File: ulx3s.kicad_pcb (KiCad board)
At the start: 4 copper layers, 94 x 50.8 mm, 119 parts, among them J1 CONN_02X20, J2 CONN_02X20, J3 WIFI_OFF, J4 CONN_02X03, Q1 BC857, Q2 2N7002, U10 S25FL164K0XMFI011, U11 PCA9306DCTR, U2 ESP-32S, U3 AP3429A, U4 AP3429A, U5 AP3429A, U6 FT231XS, U7 PCF8523, U8 MAX11123, U9 MT48LC16M16A2TG, Y1 FNETHE025

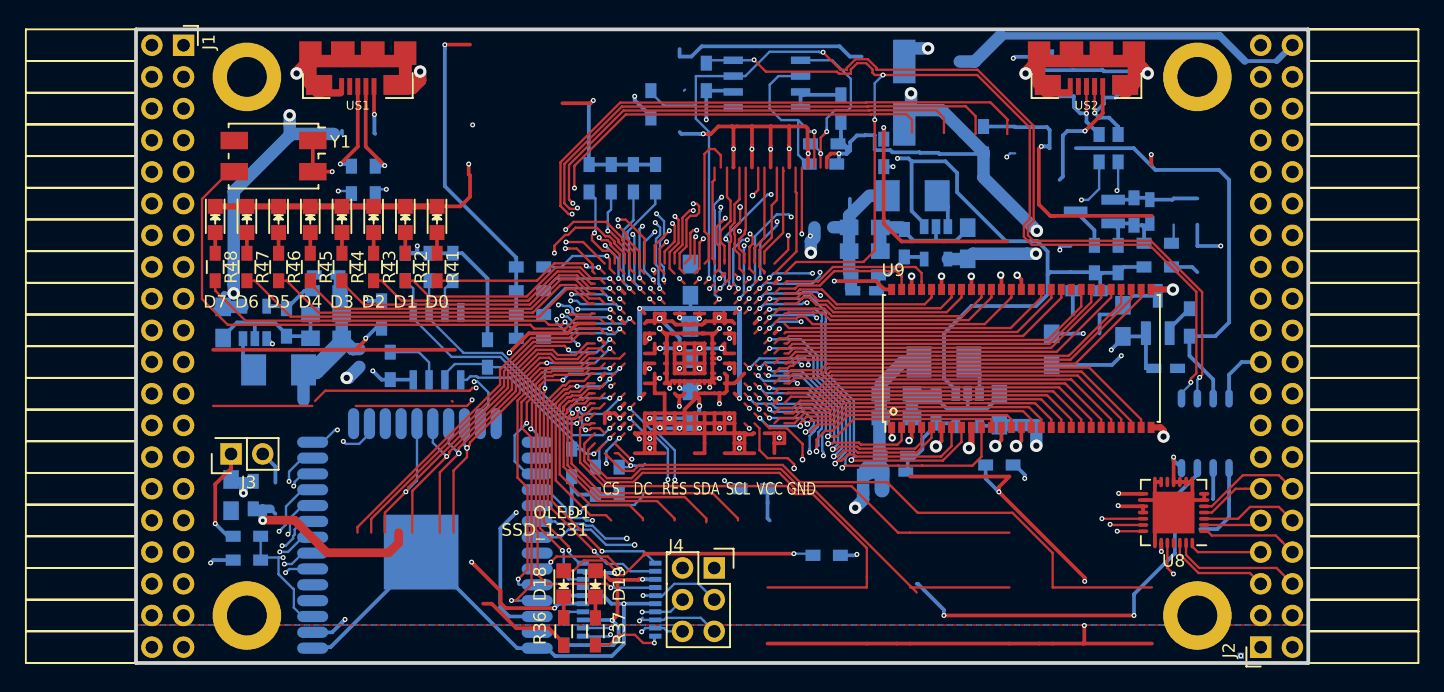
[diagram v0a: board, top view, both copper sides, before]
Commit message: HDMI fixed wrong wiring PCB v1.5 and improving copper fill areas
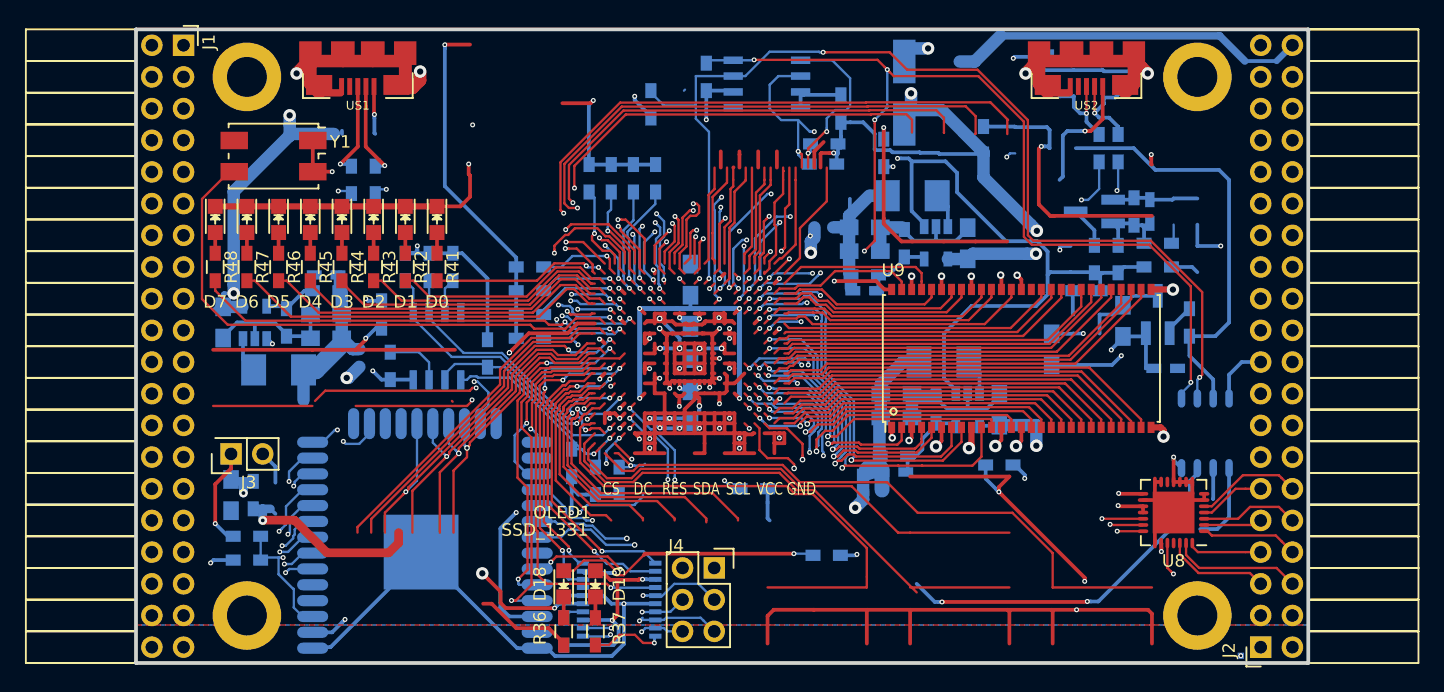
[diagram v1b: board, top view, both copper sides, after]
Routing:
- net GND: track 382.9 -> 363.4 mm, vias 58 -> 52
- net (no net): track 15.9 -> 0.05 mm
- net /blinkey/BTNPUR: track 58.0 -> 71.4 mm
- net /power/VBAT: track 32.7 -> 29.2 mm
- net GPDI_ETH+: track 11.7 -> 8.51 mm
- net +5V: track 209.2 -> 206.3 mm
- net GPDI_ETH-: track 7.83 -> 9.91 mm
- net GPDI_D2-: track 9.85 -> 8.25 mm
- net J2_25-: track 48.9 -> 47.3 mm
- net GPDI_5V_SCL: track 16.1 -> 14.7 mm, vias 1 -> 2
- net GPDI_SCL: track 86.1 -> 84.9 mm
- net GPDI_SDA: track 85.3 -> 84.8 mm, vias 4 -> 6
- net J2_27+: track 49.2 -> 48.6 mm
- net GPDI_CEC: track 9.53 -> 9.02 mm
- net GPDI_D1-: track 9.71 -> 10.0 mm, vias 2 -> 0
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
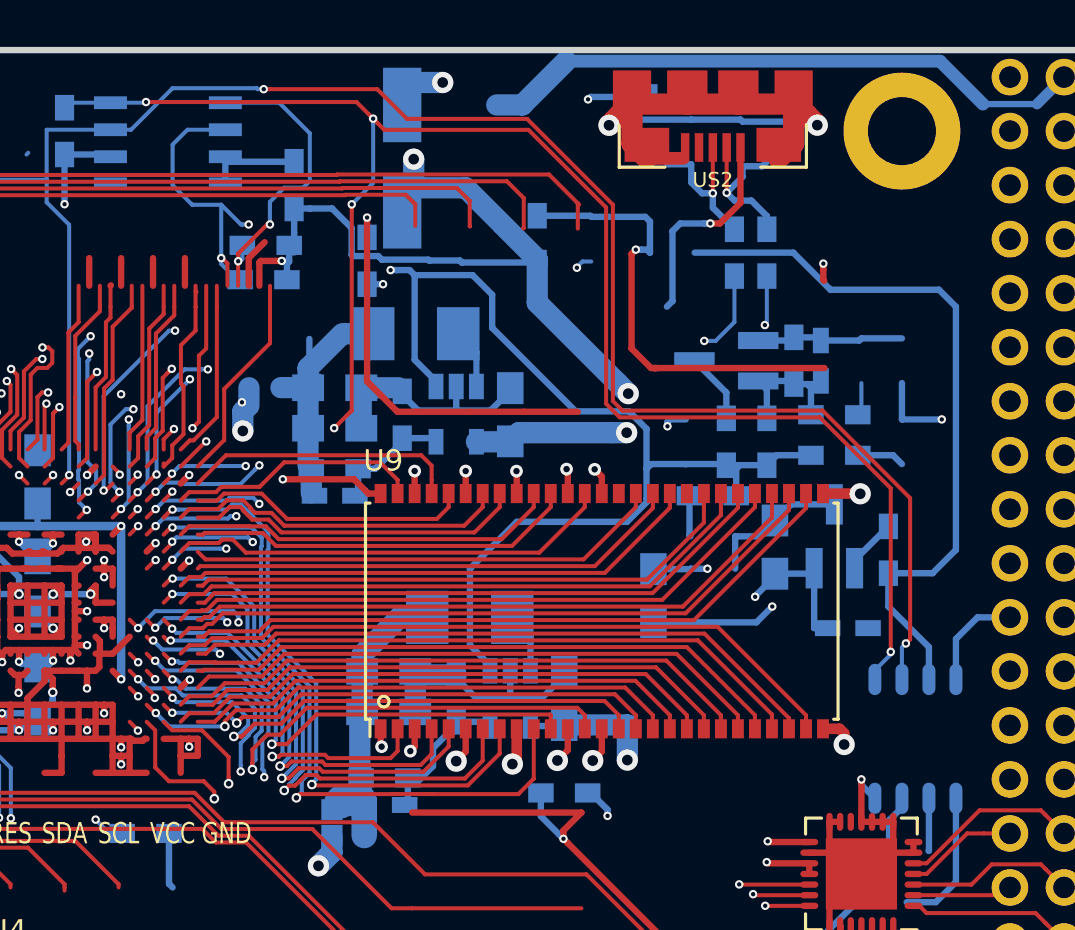
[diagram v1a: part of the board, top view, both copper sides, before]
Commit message: PCB v1.6 SDRAM fully reworked
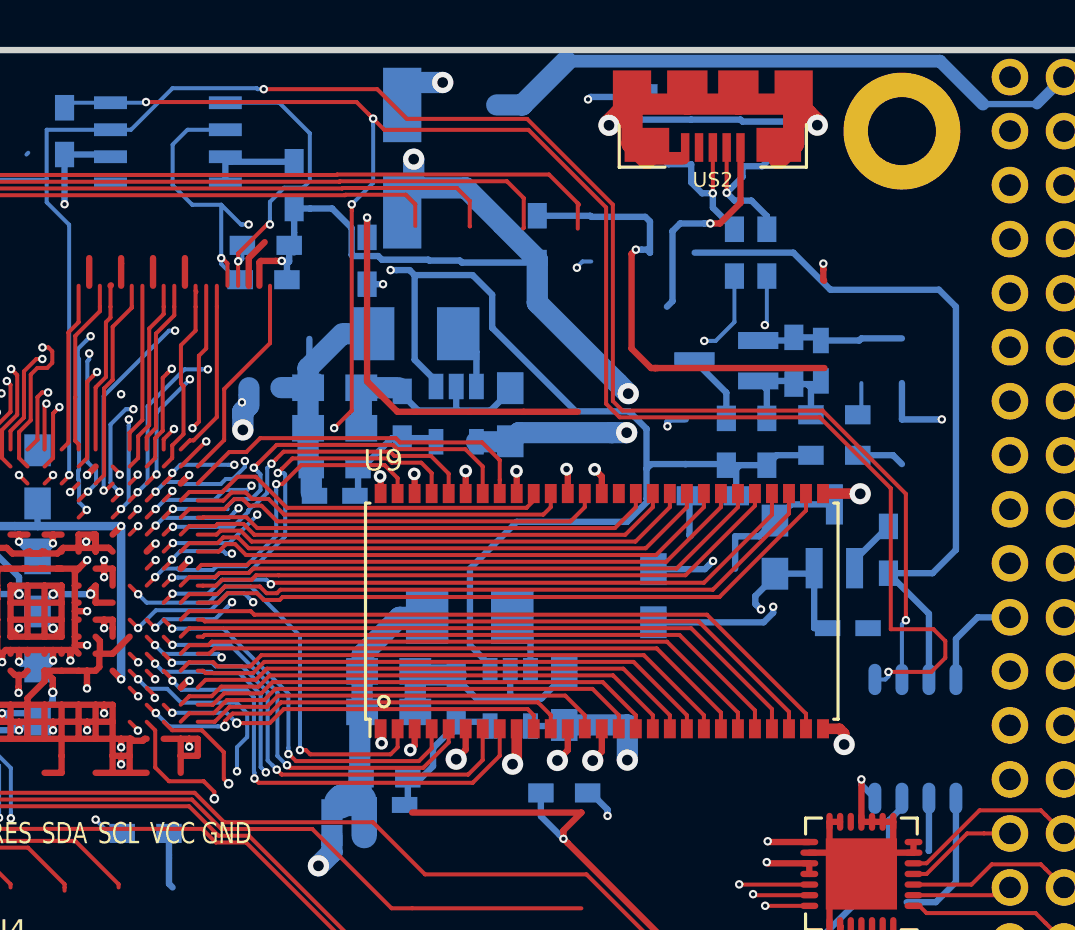
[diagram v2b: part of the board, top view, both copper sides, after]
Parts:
- U9: value MT48LC16M16A2TG -> MT48LC4M16A2TG
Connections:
- U9 pad 36: (no net) -> SDRAM_A12
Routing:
- net SDRAM_A12: track 0.00 -> 25.7 mm
- net SDRAM_D5: track 32.3 -> 18.8 mm
- net SDRAM_D4: track 29.3 -> 22.0 mm
- net SDRAM_D7: track 26.7 -> 19.7 mm, vias 2 -> 0
- net SDRAM_D3: track 26.4 -> 21.0 mm
- net SDRAM_D14: track 13.4 -> 18.7 mm, vias 0 -> 2
- net SDRAM_D15: track 11.9 -> 16.6 mm, vias 0 -> 2
- net GPDI_SDA: track 84.8 -> 89.4 mm
- net SDRAM_D2: track 23.0 -> 18.8 mm
- net GND: track 363.4 -> 359.5 mm
- net SDRAM_D13: track 13.3 -> 17.1 mm, vias 0 -> 2
- net SDRAM_D0: track 17.1 -> 20.7 mm
- net SDRAM_D12: track 16.1 -> 19.3 mm, vias 0 -> 2
- net SDRAM_DQM0: track 25.5 -> 22.4 mm, vias 2 -> 0
- net SDRAM_nCAS: track 26.3 -> 24.2 mm, vias 2 -> 0
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
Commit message: small track cosmetics
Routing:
- net GPDI_SDA: track 89.4 -> 84.9 mm
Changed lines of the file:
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@@
     (thickness 1.6)
     (drawings 28)
-    (tracks 4125)
+    (tracks 4121)
     (zones 0)
     (modules 160)
@@
   (via (at 134.48 91) (size 0.4) (drill 0.2) (layers F.Cu B.Cu) (net 14))
   (segment (start 134.88 90.6) (end 134.48 91) (width 0.3) (layer F.Cu) (net 14))
+  (segment (start 167.18355 81.105) (end 167.18355 82.68145) (width 0.3) (layer B.Cu) (net 15))
+  (segment (start 166.265 83.6) (end 161.08 83.6) (width 0.3) (layer B.Cu) (net 15))
+  (segment (start 167.18355 82.68145) (end 166.265 83.6) (width 0.3) (layer B.Cu) (net 15))
+  (segment (start 161.08 83.6) (end 158.88 85.8) (width 0.3) (layer B.Cu) (net 15))
+  (segment (start 158.88 85.8) (end 158.88 89.4) (width 0.3) (layer B.Cu) (net 15))
+  (segment (start 158.88 89.4) (end 159.825 90.345) (width 0.3) (layer B.Cu) (net 15))
+  (segment (start 159.825 90.345) (end 159.825 90.6) (width 0.3) (layer B.Cu) (net 15))
   (segment (start 121.086654 69.078528) (end 121.086654 70.584047) (width 0.3) (layer In1.Cu) (net 15))
   (segment (start 121.086654 69.078528) (end 121.1508 69.142674) (width 0.3) (layer In2.Cu) (net 15))
@@
   (segment (start 156.044535 71.764535) (end 155.432202 71.764535) (width 0.3) (layer B.Cu) (net 15))
   (segment (start 155.432202 71.764535) (end 155.14936 71.764535) (width 0.3) (layer B.Cu) (net 15))
-  (segment (start 167.18355 81.105) (end 167.18355 82.51855) (width 0.3) (layer B.Cu) (net 15))
   (segment (start 169.03 80.885) (end 167.40355 80.885) (width 0.3) (layer B.Cu) (net 15))
   (segment (start 167.40355 80.885) (end 167.18355 81.105) (width 0.3) (layer B.Cu) (net 15))
-  (segment (start 166.265 83.6) (end 167.265 82.6) (width 0.3) (layer B.Cu) (net 15))
-  (segment (start 167.18355 82.51855) (end 167.265 82.6) (width 0.3) (layer B.Cu) (net 15))
   (segment (start 156.28 75.98) (end 156.28 72) (width 0.3) (layer B.Cu) (net 15))
   (segment (start 157.285 77.235) (end 157.285 76.985) (width 0.3) (layer B.Cu) (net 15))
   (segment (start 157.285 76.985) (end 156.28 75.98) (width 0.3) (layer B.Cu) (net 15))
-  (segment (start 159.825 90.6) (end 159.825 90.345) (width 0.3) (layer B.Cu) (net 15))
-  (segment (start 159.825 90.345) (end 158.88 89.4) (width 0.3) (layer B.Cu) (net 15))
-  (segment (start 158.88 89.4) (end 158.88 85.8) (width 0.3) (layer B.Cu) (net 15))
-  (segment (start 158.88 85.8) (end 161.08 83.6) (width 0.3) (layer B.Cu) (net 15))
-  (segment (start 161.08 83.6) (end 166.265 83.6) (width 0.3) (layer B.Cu) (net 15))
   (segment (start 168.98 80.885) (end 169.03 80.885) (width 0.3) (layer B.Cu) (net 15))
   (segment (start 169.03 80.885) (end 170.885 80.885) (width 0.3) (layer B.Cu) (net 15))
@@
   (via (at 147.983153 71.34708) (size 0.4) (drill 0.2) (layers F.Cu B.Cu) (net 37))
   (via (at 149.475951 69.619684) (size 0.4) (drill 0.2) (layers F.Cu B.Cu) (net 37))
+  (segment (start 178.665908 88.648967) (end 178.55819 88.756685) (width 0.19) (layer F.Cu) (net 38))
+  (segment (start 178.55819 88.756685) (end 178.55819 90.656032) (width 0.19) (layer F.Cu) (net 38))
   (segment (start 165.918477 78.686028) (end 175.33012 78.686028) (width 0.19) (layer F.Cu) (net 38))
   (segment (start 161.633939 65.170215) (end 165.282602 68.818878) (width 0.19) (layer F.Cu) (net 38))
   (segment (start 177.92 91.011) (end 178.4148 91.011) (width 0.19) (layer B.Cu) (net 38))
-  (segment (start 181.231033 89.20607) (end 181.231033 89.99393) (width 0.19) (layer F.Cu) (net 38))
   (via (at 178.55819 90.656032) (size 0.4) (drill 0.2) (layers F.Cu B.Cu) (net 38))
   (segment (start 178.55819 90.86761) (end 178.55819 90.656032) (width 0.19) (layer B.Cu) (net 38))
-  (segment (start 178.665908 88.648967) (end 180.67393 88.648967) (width 0.19) (layer F.Cu) (net 38))
   (segment (start 178.4148 91.011) (end 178.55819 90.86761) (width 0.19) (layer B.Cu) (net 38))
   (segment (start 154.855774 65.170215) (end 161.633939 65.170215) (width 0.19) (layer F.Cu) (net 38))
   (segment (start 175.33012 78.686028) (end 178.665908 82.021816) (width 0.19) (layer F.Cu) (net 38))
   (segment (start 178.665908 82.021816) (end 178.665908 88.648967) (width 0.19) (layer F.Cu) (net 38))
-  (segment (start 180.67393 88.648967) (end 181.231033 89.20607) (width 0.19) (layer F.Cu) (net 38))
-  (segment (start 181.231033 89.99393) (end 180.568931 90.656032) (width 0.19) (layer F.Cu) (net 38))
   (segment (start 154.329326 64.643767) (end 154.855774 65.170215) (width 0.19) (layer F.Cu) (net 38))
   (segment (start 165.282602 68.818878) (end 165.282602 78.050153) (width 0.19) (layer F.Cu) (net 38))
-  (segment (start 180.568931 90.656032) (end 178.55819 90.656032) (width 0.19) (layer F.Cu) (net 38))
   (segment (start 165.282602 78.050153) (end 165.918477 78.686028) (width 0.19) (layer F.Cu) (net 38))
   (segment (start 148.2539 80.000797) (end 148.254705 79.999992) (width 0.19) (layer In2.Cu) (net 38))
@@
   (segment (start 141.98 63.895) (end 140.055 63.895) (width 0.19) (layer B.Cu) (net 38))
   (segment (start 140.055 63.895) (end 139.82 64.13) (width 0.19) (layer B.Cu) (net 38))
-  (segment (start 179.19 91.011) (end 179.19 88.412934) (width 0.19) (layer B.Cu) (net 39))
-  (via (at 179.375977 88.226957) (size 0.4) (drill 0.2) (layers F.Cu B.Cu) (net 39))
+  (segment (start 149.183754 63.257114) (end 154.004817 63.257114) (width 0.19) (layer F.Cu) (net 39))
   (segment (start 165.599613 77.918843) (end 166.049787 78.369017) (width 0.19) (layer F.Cu) (net 39))
-  (segment (start 179.19 88.412934) (end 179.375977 88.226957) (width 0.19) (layer B.Cu) (net 39))
-  (segment (start 154.520337 63.257114) (end 155.918329 64.655106) (width 0.19) (layer F.Cu) (net 39))
-  (segment (start 161.567151 64.655106) (end 165.599613 68.687568) (width 0.19) (layer F.Cu) (net 39))
+  (segment (start 154.004817 63.257114) (end 155.402809 64.655106) (width 0.19) (layer F.Cu) (net 39))
   (segment (start 175.46143 78.369017) (end 179.375977 82.283564) (width 0.19) (layer F.Cu) (net 39))
-  (segment (start 179.375977 82.283564) (end 179.375977 87.944115) (width 0.19) (layer F.Cu) (net 39))
   (segment (start 179.375977 87.944115) (end 179.375977 88.226957) (width 0.19) (layer F.Cu) (net 39))
-  (segment (start 166.049787 78.369017) (end 175.46143 78.369017) (width 0.19) (layer F.Cu) (net 39))
-  (segment (start 155.918329 64.655106) (end 161.567151 64.655106) (width 0.19) (layer F.Cu) (net 39))
+  (segment (start 155.402809 64.655106) (end 161.567151 64.655106) (width 0.19) (layer F.Cu) (net 39))
+  (segment (start 161.567151 64.655106) (end 165.599613 68.687568) (width 0.19) (layer F.Cu) (net 39))
   (segment (start 165.599613 68.687568) (end 165.599613 77.918843) (width 0.19) (layer F.Cu) (net 39))
-  (segment (start 149.183754 63.257114) (end 154.520337 63.257114) (width 0.19) (layer F.Cu) (net 39))
+  (segment (start 166.049787 78.369017) (end 175.46143 78.369017) (width 0.19) (layer F.Cu) (net 39))
+  (segment (start 179.375977 82.283564) (end 179.375977 87.944115) (width 0.19) (layer F.Cu) (net 39))
+  (segment (start 179.19 91.011) (end 179.19 88.412934) (width 0.19) (layer B.Cu) (net 39))
+  (via (at 179.375977 88.226957) (size 0.4) (drill 0.2) (layers F.Cu B.Cu) (net 39))
+  (segment (start 179.19 88.412934) (end 179.375977 88.226957) (width 0.19) (layer B.Cu) (net 39))
   (segment (start 138.98 68.578574) (end 138.98 67.516) (width 0.19) (layer B.Cu) (net 39))
   (segment (start 140.035989 81.4) (end 140.035989 69.634563) (width 0.19) (layer B.Cu) (net 39))

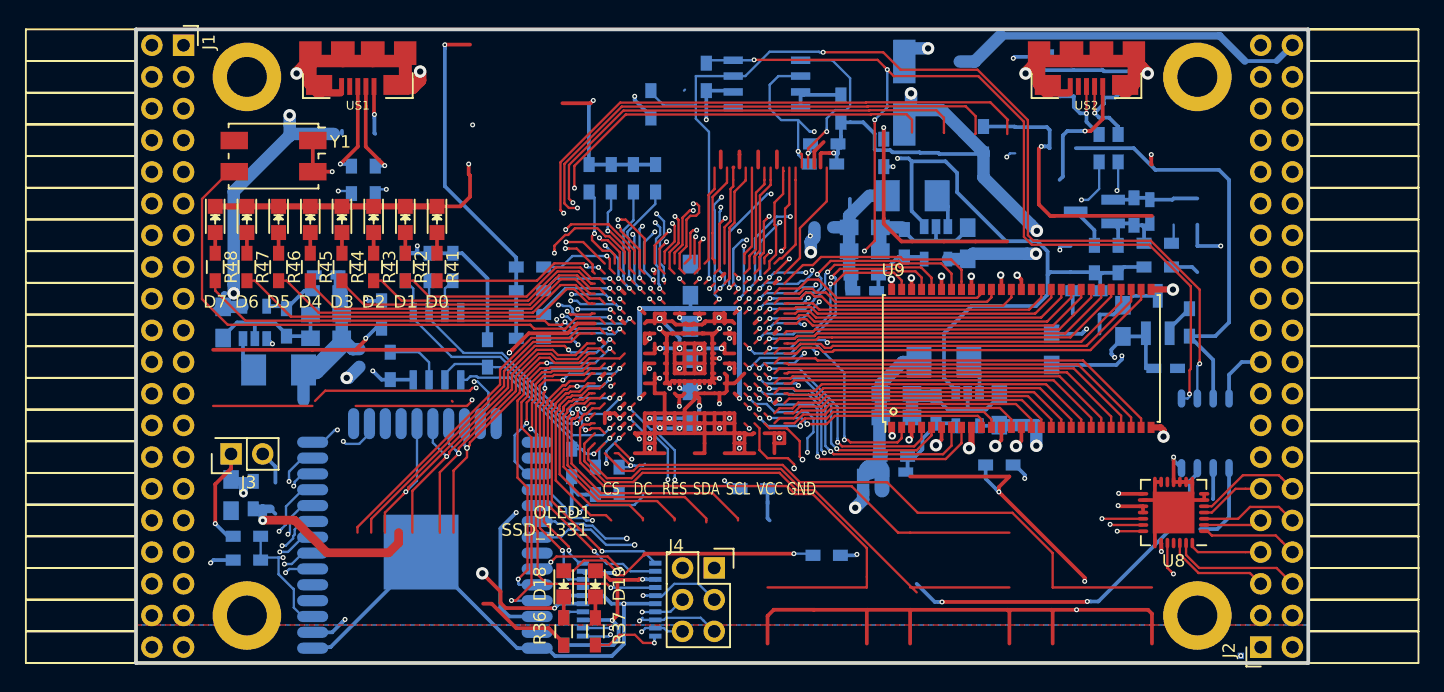
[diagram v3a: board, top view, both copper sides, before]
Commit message: small trace/via thickening and cosmetic edits
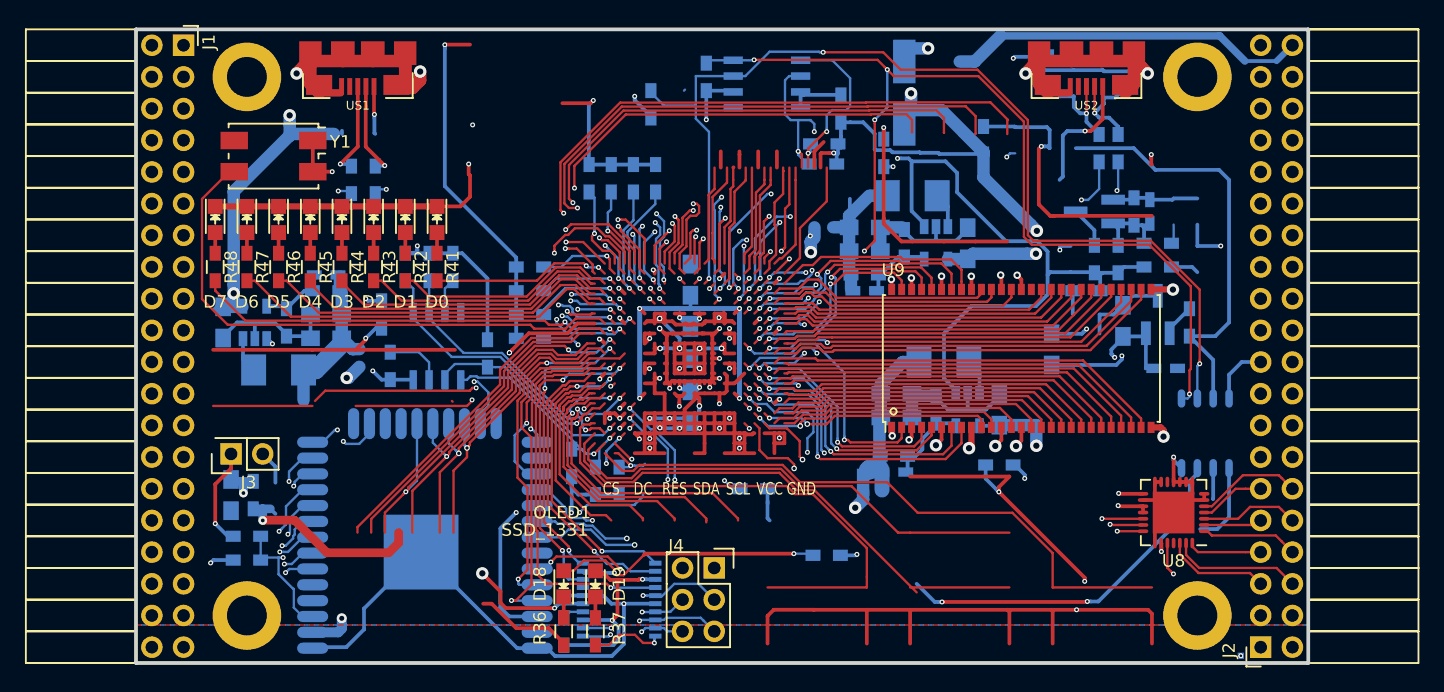
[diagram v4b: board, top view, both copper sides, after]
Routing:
- net GPDI_5V_SCL: track 14.7 -> 13.1 mm
- net GND: track 359.5 -> 360.3 mm
